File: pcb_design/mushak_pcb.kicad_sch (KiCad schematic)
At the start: 49 parts, among them J1 Conn_01x04_Male, J10 IR_1, J11 AS5600_1, J12 IR_2, J13 AS5600_2, J14 IR_3, J15 ToF, J16 IR_4, J2 Conn_01x02_Female, J3 BLE_Conn, Q1 DMN3065LW-7, SW1 SW_Push, SW2 SW_Push, U1 BA30BC0FP-E2, U6 STM32F405RGTx, Y1 25Mhz, Y2 32.769kHz

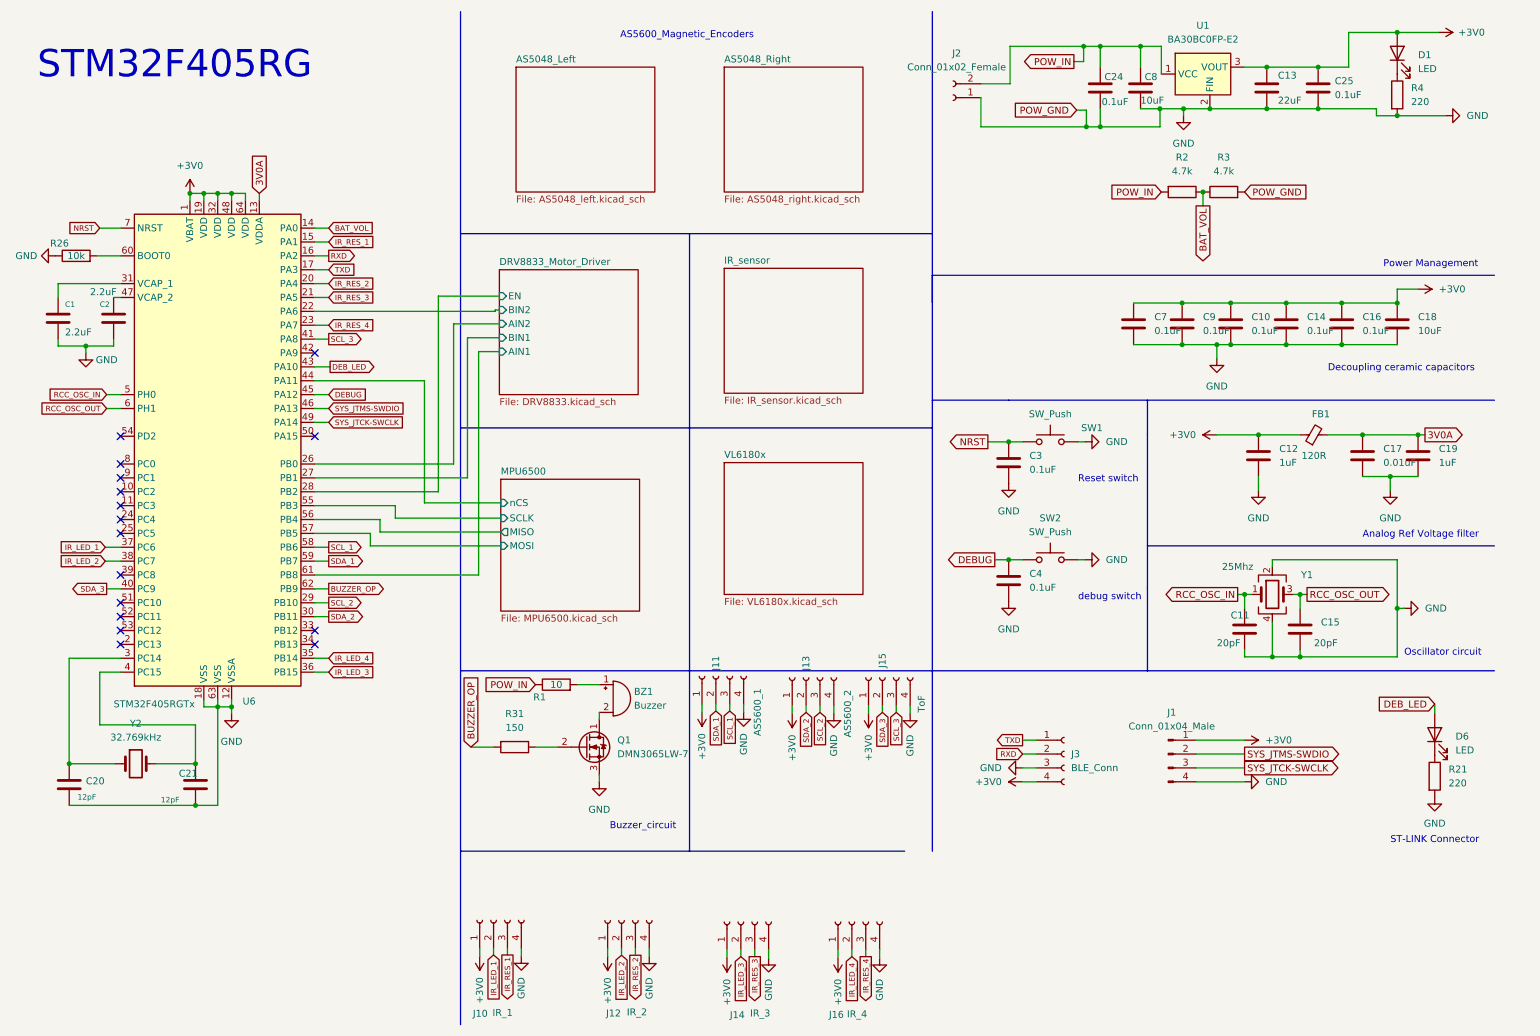
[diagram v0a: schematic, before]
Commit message: Update mushak PCB with new changes * Add AMS1117 as 3.3v regulator * Add new alternate placement for IR sensors * Add new 3.3v compatible ToF sensor * Update gerber files
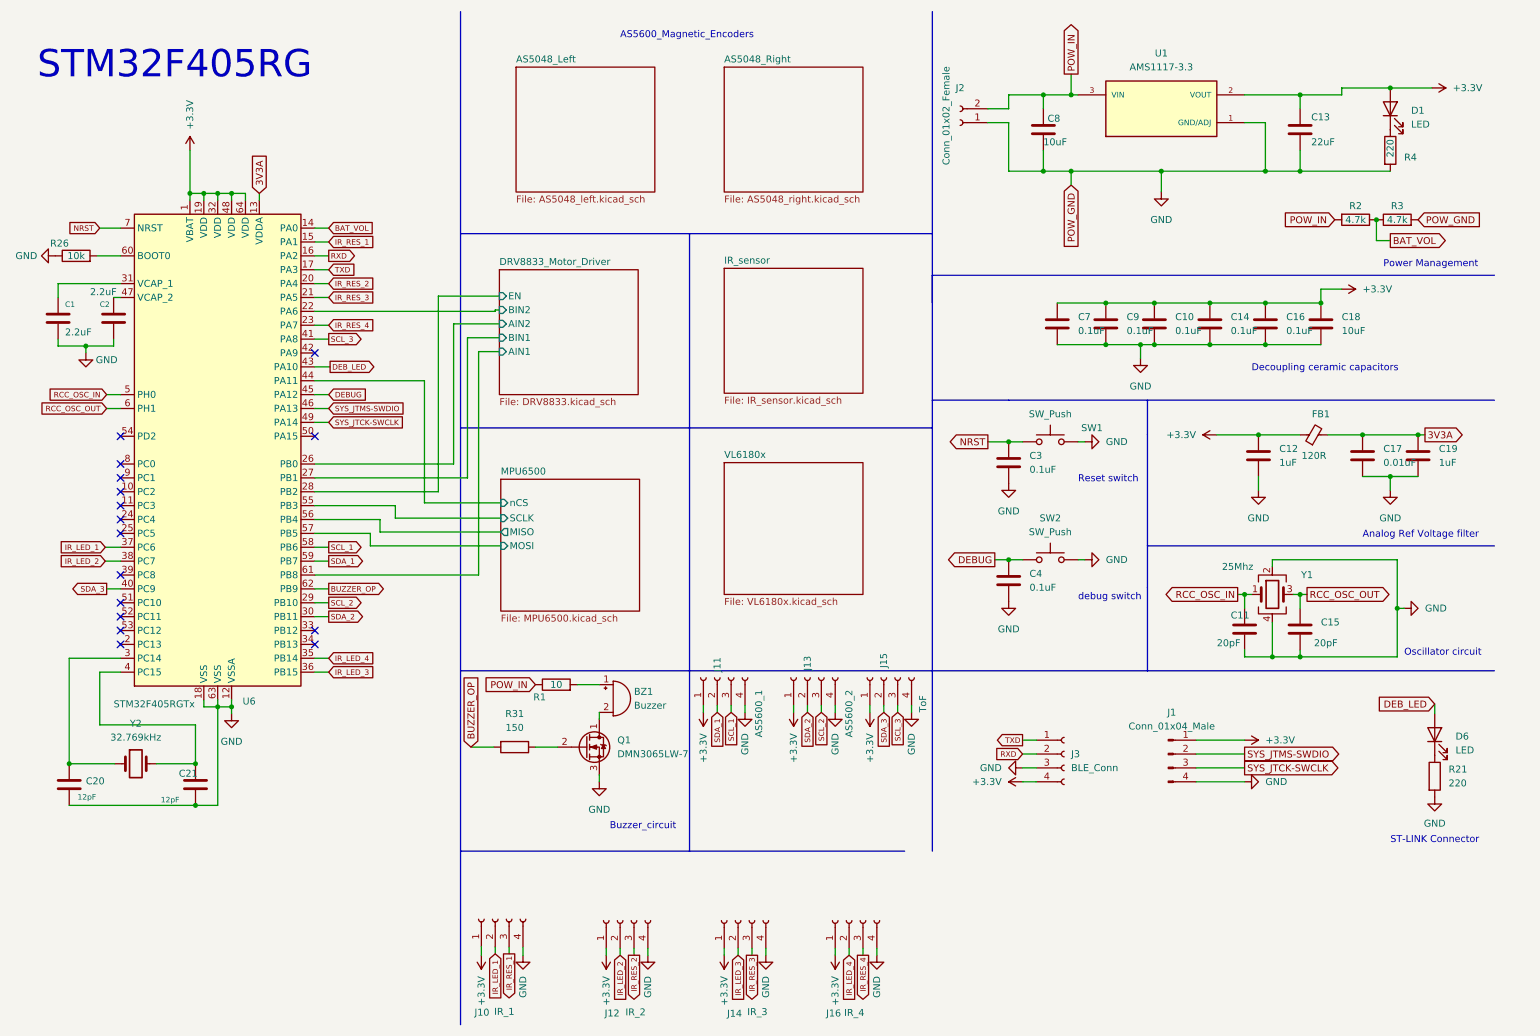
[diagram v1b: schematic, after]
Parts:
- removed C24, C25: 0.1uF, Capacitor_SMD:C_0402_1005Metric, symbol Device:C
- removed U1: BA30BC0FP-E2, IPD50P04P4L-11:DPAK228P998X235-3N, symbol BA30BC0FP-E2:BA30BC0FP-E2
- added U1: AMS1117-3.3, AMS1117-3:SOT229P700X180-4N, symbol AMS1117-3.3:AMS1117-3.3
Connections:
- net GND: now also U1.1 (GND/ADJ)
- net POW_IN: now also U1.3 (VIN)
- net +3V0 renamed +3.3V
- net +3.3V: now also U1.2 (VOUT)
- net 3V0A renamed 3V3A
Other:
- moved on the sheet: C10, C13, C14, C16, C18, C7, C8, C9, D1, J14, J16, J2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
